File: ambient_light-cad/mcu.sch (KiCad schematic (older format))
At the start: 22 parts

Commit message: [Modified] +5V to VCC /interface
전에 USBVCC와 레귤레이터 5V 분리를 위해서 섞인 VCC와 +5V를 단일화 시킴
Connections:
- net labels removed: +5V
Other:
- moved on the sheet: C?, D?, SW?, U?, Y?

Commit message: [Modified] Register symbol
R_Small to R_Small_US (구불구불하게 생긴 기호)
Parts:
- added U?: NE555D, Package_SO:SOIC-8_3.9x4.9mm_P1.27mm, symbol Timer:NE555D
- R? (x6): symbol Device:R_Small -> Device:R_Small_US
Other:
- moved on the sheet: C?, Y?
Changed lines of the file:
@@
 L power:GND #PWR?
 U 1 1 5FD4BFB2
-P 7700 4250
+P 1950 7150
 AR Path="/5FD4BFB2" Ref="#PWR?"  Part="1"
 AR Path="/5FD145BE/5FD4BFB2" Ref="#PWR?"  Part="1"
-F 0 "#PWR?" H 7700 4000 50  0001 C CNN
-F 1 "GND" H 7705 4077 50  0000 C CNN
-F 2 "" H 7700 4250 50  0001 C CNN
-F 3 "" H 7700 4250 50  0001 C CNN
-	1    7700 4250
-	1    0    0    -1
-$EndComp
-Text Label 6700 3300 0    50   ~ 0
+F 0 "#PWR?" H 1950 6900 50  0001 C CNN
+F 1 "GND" H 1955 6977 50  0000 C CNN
+F 2 "" H 1950 7150 50  0001 C CNN
+F 3 "" H 1950 7150 50  0001 C CNN
+	1    1950 7150
+	1    0    0    -1
+$EndComp
+Text Label 950  6200 0    50   ~ 0
 XTAL1
-Text Label 6700 3400 0    50   ~ 0
+Text Label 950  6300 0    50   ~ 0
 XTAL2
 Wire Wire Line
-	7300 2900 7700 2900
-Wire Wire Line
-	7300 3300 6700 3300
-Wire Wire Line
-	7700 2900 7700 3400
-Wire Wire Line
-	7700 3400 6700 3400
-Connection ~ 7300 3300
-Connection ~ 7700 3400
-Wire Wire Line
-	7100 3100 7100 4050
-Wire Wire Line
-	7100 4050 7300 4050
-Connection ~ 7300 4050
-Wire Wire Line
-	7300 4050 7500 4050
-Wire Wire Line
-	7500 3100 7500 4050
-Connection ~ 7500 4050
-Wire Wire Line
-	7500 4050 7700 4050
-Wire Wire Line
-	7700 4050 7700 4250
-Connection ~ 7700 4050
+	1550 5800 1950 5800
+Wire Wire Line
+	1550 6200 950  6200
+Wire Wire Line
+	1950 5800 1950 6300
+Wire Wire Line
+	1950 6300 950  6300
+Connection ~ 1550 6200
+Connection ~ 1950 6300
+Wire Wire Line
+	1350 6000 1350 6950
+Wire Wire Line
+	1350 6950 1550 6950
+Connection ~ 1550 6950
+Wire Wire Line
+	1550 6950 1750 6950
+Wire Wire Line
+	1750 6000 1750 6950
+Connection ~ 1750 6950
+Wire Wire Line
+	1750 6950 1950 6950
+Wire Wire Line
+	1950 6950 1950 7150
+Connection ~ 1950 6950
 $Comp
 L Interface_USB:CH340G U?
@@
 $EndComp
 $Comp
-L Device:R_Small R?
+L Device:R_Small_US R?
 U 1 1 5FD4C06D
 P 3900 2000
@@
 L Device:Crystal_GND24_Small Y?
 U 1 1 5FD4C073
-P 7300 3100
+P 1550 6000
 AR Path="/5FD4C073" Ref="Y?"  Part="1"
 AR Path="/5FD145BE/5FD4C073" Ref="Y?"  Part="1"
-F 0 "Y?" V 7100 2600 50  0000 L CNN
-F 1 "14.4756MHz" V 7200 2600 50  0000 L CNN
-F 2 "" H 7300 3100 50  0001 C CNN
-F 3 "~" H 7300 3100 50  0001 C CNN
-	1    7300 3100
+F 0 "Y?" V 1350 5500 50  0000 L CNN
+F 1 "14.4756MHz" V 1450 5500 50  0000 L CNN
+F 2 "" H 1550 6000 50  0001 C CNN
+F 3 "~" H 1550 6000 50  0001 C CNN
+	1    1550 6000
 	0    1    1    0
 $EndComp
@@
 	0    -1   -1   0
 $EndComp
-$Comp
-L Device:R_Small R?
-U 1 1 5FD4C07F
-P 3900 2100
-AR Path="/5FD4C07F" Ref="R?"  Part="1"
-AR Path="/5FD145BE/5FD4C07F" Ref="R?"  Part="1"
-F 0 "R?" V 4000 2050 50  0000 C CNN
-F 1 "1k" V 4000 2150 50  0000 C CNN
-F 2 "" H 3900 2100 50  0001 C CNN
-F 3 "~" H 3900 2100 50  0001 C CNN
-	1    3900 2100
-	0    1    1    0
-$EndComp
 Wire Wire Line
 	3500 2000 3800 2000
@@
 	4000 2000 4150 2000
 $Comp
-L Device:R_Small R?
+L Device:R_Small_US R?
 U 1 1 5FD4C089
 P 4300 1300
@@
 $EndComp
 $Comp
-L Device:R_Small R?
+L Device:R_Small_US R?
 U 1 1 5FD4C08F
 P 4150 1300
@@
 	4150 1150 4150 1200
 $Comp
-L Device:R_Small R?
+L Device:R_Small_US R?
 U 1 1 5FD4C097
 P 5900 5250
@@
 Wire Wire Line
 	3500 2700 3700 2700
-Wire Wire Line
-	3900 2700 4100 2700
 $Comp
 L Device:C_Small C?
 U 1 1 5FD4C0D2
-P 7300 3700
+P 1550 6600
 AR Path="/5FD4C0D2" Ref="C?"  Part="1"
 AR Path="/5FD145BE/5FD4C0D2" Ref="C?"  Part="1"
-F 0 "C?" H 7400 3700 50  0000 L CNN
-F 1 "18pF" H 7300 3600 50  0000 L CNN
-F 2 "" H 7300 3700 50  0001 C CNN
-F 3 "~" H 7300 3700 50  0001 C CNN
-	1    7300 3700
+F 0 "C?" H 1650 6600 50  0000 L CNN
+F 1 "18pF" H 1550 6500 50  0000 L CNN
+F 2 "" H 1550 6600 50  0001 C CNN
+F 3 "~" H 1550 6600 50  0001 C CNN
+	1    1550 6600
 	1    0    0    -1
 $EndComp
@@
 L Device:C_Small C?
 U 1 1 5FD4C0D8
-P 7700 3700
+P 1950 6600
 AR Path="/5FD4C0D8" Ref="C?"  Part="1"
 AR Path="/5FD145BE/5FD4C0D8" Ref="C?"  Part="1"
-F 0 "C?" H 7800 3700 50  0000 L CNN
-F 1 "18pF" H 7700 3600 50  0000 L CNN
-F 2 "" H 7700 3700 50  0001 C CNN
-F 3 "~" H 7700 3700 50  0001 C CNN
-	1    7700 3700
-	1    0    0    -1
-$EndComp
-Wire Wire Line
-	7300 3300 7300 3600
-Wire Wire Line
-	7300 3800 7300 4050
-Wire Wire Line
-	7700 3400 7700 3600
-Wire Wire Line
-	7700 3800 7700 4050
-Wire Wire Line
-	7300 3200 7300 3300
-Wire Wire Line
-	7100 3100 7200 3100
-Wire Wire Line
-	7400 3100 7500 3100
-Wire Wire Line
-	7300 2900 7300 3000
+F 0 "C?" H 2050 6600 50  0000 L CNN
+F 1 "18pF" H 1950 6500 50  0000 L CNN
+F 2 "" H 1950 6600 50  0001 C CNN
+F 3 "~" H 1950 6600 50  0001 C CNN
+	1    1950 6600
+	1    0    0    -1
+$EndComp
+Wire Wire Line
+	1550 6200 1550 6500
+Wire Wire Line
+	1550 6700 1550 6950
+Wire Wire Line
+	1950 6300 1950 6500
+Wire Wire Line
+	1950 6700 1950 6950
+Wire Wire Line
+	1550 6100 1550 6200
+Wire Wire Line
+	1350 6000 1450 6000
+Wire Wire Line
+	1650 6000 1750 6000
+Wire Wire Line
+	1550 5800 1550 5900
 $Comp
 L Device:Crystal_GND24_Small Y?
@@
 	1650 1900 1750 1900
 $Comp
-L Device:R_Small R?
+L Device:R_Small_US R?
 U 1 1 5FD4C0F0
 P 1350 4100
@@
 	1    0    0    -1
 $EndComp
+$Comp
+L Timer:NE555D U?
+U 1 1 5FE4F839
+P 8100 2550
+F 0 "U?" H 7850 2150 50  0000 C CNN
+F 1 "NE555D" H 7850 2050 50  0000 C CNN
+F 2 "Package_SO:SOIC-8_3.9x4.9mm_P1.27mm" H 8950 2150 50  0001 C CNN
+F 3 "http://www.ti.com/lit/ds/symlink/ne555.pdf" H 8950 2150 50  0001 C CNN
+	1    8100 2550
+	1    0    0    -1
+$EndComp
+$Comp
+L power:VCC #PWR?
+U 1 1 5FE4FEF0
+P 8100 1750
+F 0 "#PWR?" H 8100 1600 50  0001 C CNN
+F 1 "VCC" H 8115 1923 50  0000 C CNN
+F 2 "" H 8100 1750 50  0001 C CNN
+F 3 "" H 8100 1750 50  0001 C CNN
+	1    8100 1750
+	1    0    0    -1
+$EndComp
+$Comp
+L power:GND #PWR?
+U 1 1 5FE50BA2
+P 8100 3150
+F 0 "#PWR?" H 8100 2900 50  0001 C CNN
+F 1 "GND" H 8105 2977 50  0000 C CNN
+F 2 "" H 8100 3150 50  0001 C CNN
+F 3 "" H 8100 3150 50  0001 C CNN
+	1    8100 3150
+	1    0    0    -1
+$EndComp
+Wire Wire Line
+	3900 2700 4100 2700
+$Comp
+L Device:R_Small_US R?
+U 1 1 5FD4C07F
+P 3900 2100
+AR Path="/5FD4C07F" Ref="R?"  Part="1"
+AR Path="/5FD145BE/5FD4C07F" Ref="R?"  Part="1"
+F 0 "R?" V 4000 2050 50  0000 C CNN
+F 1 "1k" V 4000 2150 50  0000 C CNN
+F 2 "" H 3900 2100 50  0001 C CNN
+F 3 "~" H 3900 2100 50  0001 C CNN
+	1    3900 2100
+	0    1    1    0
+$EndComp
 $EndSCHEMATC

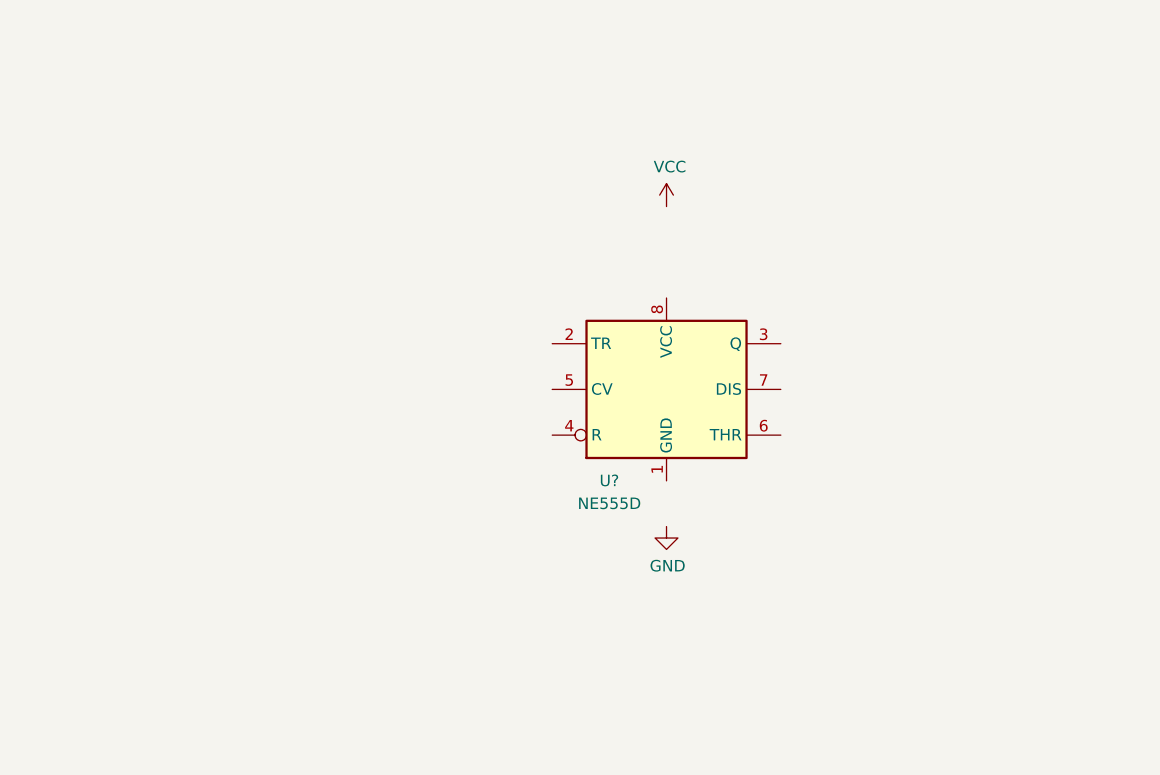
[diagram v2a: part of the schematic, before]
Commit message: [Added] NE555 Reset Setting button
CH340G DTR pin과 ATmega328P Rst pin 을 일시적으로 연결시키기 위한 10sec NE555 Monostable 로직 구현
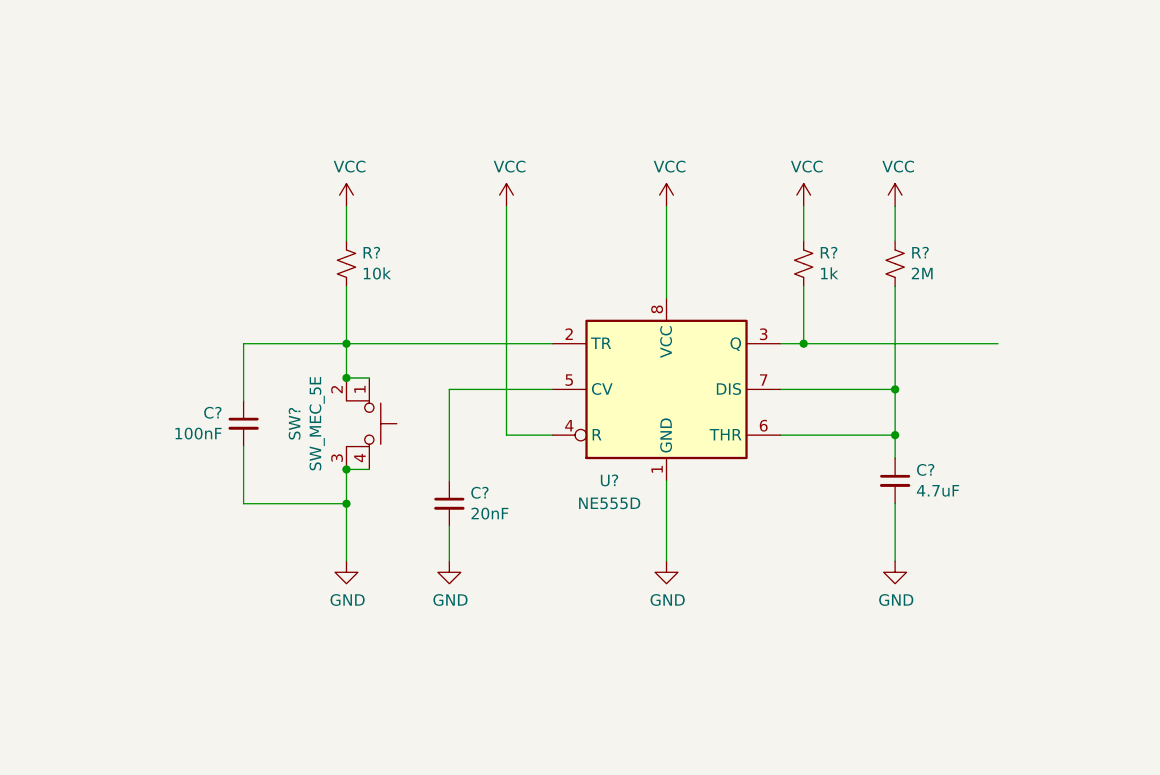
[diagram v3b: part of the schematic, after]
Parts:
- added C?: 20nF, symbol Device:C_Small
- added C?: 4.7uF, symbol Device:C_Small
- added C?: 100nF, symbol Device:C_Small
- added R?: 10k, symbol Device:R_Small_US
- added R?: 2M, symbol Device:R_Small_US
- added R?: 1k, symbol Device:R_Small_US
- added SW?: SW_MEC_5E, symbol Switch:SW_MEC_5E
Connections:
- net GND: now also U?.1 (GND), C?.2, C?.2, C?.2, SW?.3 (K), SW?.4 (A)
- net VCC: now also U?.4 (R), U?.8 (VCC), R?.1, R?.1, R?.1
- net at U?.2 (TR): now also C?.1, R?.2, SW?.1, SW?.2
- net at U?.3 (Q): now also R?.2
- net at U?.5 (CV): now also C?.1
- net at U?.6 (THR): now also U?.7 (DIS), C?.1, R?.2
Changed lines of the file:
@@
-$EndComp
-$Comp
-L Timer:NE555D U?
-U 1 1 5FE4F839
-P 8100 2550
-F 0 "U?" H 7850 2150 50  0000 C CNN
-F 1 "NE555D" H 7850 2050 50  0000 C CNN
-F 2 "Package_SO:SOIC-8_3.9x4.9mm_P1.27mm" H 8950 2150 50  0001 C CNN
-F 3 "http://www.ti.com/lit/ds/symlink/ne555.pdf" H 8950 2150 50  0001 C CNN
-	1    8100 2550
-	1    0    0    -1
 $EndComp
 $Comp
@@
 L power:GND #PWR?
 U 1 1 5FE50BA2
-P 8100 3150
-F 0 "#PWR?" H 8100 2900 50  0001 C CNN
-F 1 "GND" H 8105 2977 50  0000 C CNN
-F 2 "" H 8100 3150 50  0001 C CNN
-F 3 "" H 8100 3150 50  0001 C CNN
-	1    8100 3150
+P 8100 3300
+F 0 "#PWR?" H 8100 3050 50  0001 C CNN
+F 1 "GND" H 8105 3127 50  0000 C CNN
+F 2 "" H 8100 3300 50  0001 C CNN
+F 3 "" H 8100 3300 50  0001 C CNN
+	1    8100 3300
 	1    0    0    -1
 $EndComp
@@
 	0    1    1    0
 $EndComp
+$Comp
+L Device:R_Small_US R?
+U 1 1 5FE64F71
+P 6700 2000
+F 0 "R?" H 6768 2046 50  0000 L CNN
+F 1 "10k" H 6768 1955 50  0000 L CNN
+F 2 "" H 6700 2000 50  0001 C CNN
+F 3 "~" H 6700 2000 50  0001 C CNN
+	1    6700 2000
+	1    0    0    -1
+$EndComp
+$Comp
+L Device:C_Small C?
+U 1 1 5FE7649B
+P 7150 3050
+F 0 "C?" H 7242 3096 50  0000 L CNN
+F 1 "20nF" H 7242 3005 50  0000 L CNN
+F 2 "" H 7150 3050 50  0001 C CNN
+F 3 "~" H 7150 3050 50  0001 C CNN
+	1    7150 3050
+	1    0    0    -1
+$EndComp
+$Comp
+L Device:R_Small_US R?
+U 1 1 5FE80D08
+P 8700 2000
+F 0 "R?" H 8768 2046 50  0000 L CNN
+F 1 "1k" H 8768 1955 50  0000 L CNN
+F 2 "" H 8700 2000 50  0001 C CNN
+F 3 "~" H 8700 2000 50  0001 C CNN
+	1    8700 2000
+	1    0    0    -1
+$EndComp
+Wire Wire Line
+	8100 2950 8100 3300
+$Comp
+L power:GND #PWR?
+U 1 1 5FEB39CC
+P 7150 3300
+F 0 "#PWR?" H 7150 3050 50  0001 C CNN
+F 1 "GND" H 7155 3127 50  0000 C CNN
+F 2 "" H 7150 3300 50  0001 C CNN
+F 3 "" H 7150 3300 50  0001 C CNN
+	1    7150 3300
+	1    0    0    -1
+$EndComp
+Wire Wire Line
+	7150 3300 7150 3150
+Wire Wire Line
+	7150 2950 7150 2550
+$Comp
+L Switch:SW_MEC_5E SW?
+U 1 1 5FE63505
+P 6700 2700
+F 0 "SW?" H 6700 2475 50  0000 C CNN
+F 1 "SW_MEC_5E" H 6700 2566 50  0000 C CNN
+F 2 "" H 6700 3000 50  0001 C CNN
+F 3 "http://www.apem.com/int/index.php?controller=attachment&id_attachment=1371" H 6700 3000 50  0001 C CNN
+	1    6700 2700
+	0    1    1    0
+$EndComp
+$Comp
+L Timer:NE555D U?
+U 1 1 5FE4F839
+P 8100 2550
+F 0 "U?" H 7850 2150 50  0000 C CNN
+F 1 "NE555D" H 7850 2050 50  0000 C CNN
+F 2 "Package_SO:SOIC-8_3.9x4.9mm_P1.27mm" H 8950 2150 50  0001 C CNN
+F 3 "http://www.ti.com/lit/ds/symlink/ne555.pdf" H 8950 2150 50  0001 C CNN
+	1    8100 2550
+	1    0    0    -1
+$EndComp
+Wire Wire Line
+	8100 1750 8100 2150
+Wire Wire Line
+	6700 2100 6700 2350
+Wire Wire Line
+	7600 2350 6700 2350
+Connection ~ 6700 2350
+Wire Wire Line
+	6700 2350 6700 2500
+$Comp
+L power:GND #PWR?
+U 1 1 5FF1BCD1
+P 6700 3300
+F 0 "#PWR?" H 6700 3050 50  0001 C CNN
+F 1 "GND" H 6705 3127 50  0000 C CNN
+F 2 "" H 6700 3300 50  0001 C CNN
+F 3 "" H 6700 3300 50  0001 C CNN
+	1    6700 3300
+	1    0    0    -1
+$EndComp
+Wire Wire Line
+	6700 2900 6700 3050
+$Comp
+L power:VCC #PWR?
+U 1 1 5FF26EBE
+P 6700 1750
+F 0 "#PWR?" H 6700 1600 50  0001 C CNN
+F 1 "VCC" H 6715 1923 50  0000 C CNN
+F 2 "" H 6700 1750 50  0001 C CNN
+F 3 "" H 6700 1750 50  0001 C CNN
+	1    6700 1750
+	1    0    0    -1
+$EndComp
+Wire Wire Line
+	6700 1750 6700 1900
+Wire Wire Line
+	6700 2500 6800 2500
+Connection ~ 6700 2500
+Wire Wire Line
+	6700 2900 6800 2900
+Connection ~ 6700 2900
+$Comp
+L Device:C_Small C?
+U 1 1 5FF36A63
+P 6250 2700
+F 0 "C?" H 6342 2746 50  0000 L CNN
+F 1 "100nF" H 6342 2655 50  0000 L CNN
+F 2 "" H 6250 2700 50  0001 C CNN
+F 3 "~" H 6250 2700 50  0001 C CNN
+	1    6250 2700
+	-1   0    0    -1
+$EndComp
+Wire Wire Line
+	6250 2800 6250 3050
+Wire Wire Line
+	6250 3050 6700 3050
+Connection ~ 6700 3050
+Wire Wire Line
+	6700 3050 6700 3300
+Wire Wire Line
+	6250 2600 6250 2350
+Wire Wire Line
+	6250 2350 6700 2350
+$Comp
+L power:VCC #PWR?
+U 1 1 5FF5892D
+P 7400 1750
+F 0 "#PWR?" H 7400 1600 50  0001 C CNN
+F 1 "VCC" H 7415 1923 50  0000 C CNN
+F 2 "" H 7400 1750 50  0001 C CNN
+F 3 "" H 7400 1750 50  0001 C CNN
+	1    7400 1750
+	1    0    0    -1
+$EndComp
+Wire Wire Line
+	7150 2550 7600 2550
+Wire Wire Line
+	7400 2750 7600 2750
+Wire Wire Line
+	7400 1750 7400 2750
+$Comp
+L power:VCC #PWR?
+U 1 1 5FF698E0
+P 8700 1750
+F 0 "#PWR?" H 8700 1600 50  0001 C CNN
+F 1 "VCC" H 8715 1923 50  0000 C CNN
+F 2 "" H 8700 1750 50  0001 C CNN
+F 3 "" H 8700 1750 50  0001 C CNN
+	1    8700 1750
+	1    0    0    -1
+$EndComp
+Wire Wire Line
+	8700 1900 8700 1750
+Wire Wire Line
+	8700 2100 8700 2350
+Connection ~ 8700 2350
+Wire Wire Line
+	8700 2350 8600 2350
+Wire Wire Line
+	8700 2350 9550 2350
+Wire Wire Line
+	9100 3050 9100 3300
+Wire Wire Line
+	9100 2750 9100 2850
+Connection ~ 9100 2750
+Wire Wire Line
+	9100 2550 9100 2750
+Wire Wire Line
+	8600 2750 9100 2750
+Wire Wire Line
+	8600 2550 9100 2550
+$Comp
+L power:GND #PWR?
+U 1 1 5FE84EAC
+P 9100 3300
+F 0 "#PWR?" H 9100 3050 50  0001 C CNN
+F 1 "GND" H 9105 3127 50  0000 C CNN
+F 2 "" H 9100 3300 50  0001 C CNN
+F 3 "" H 9100 3300 50  0001 C CNN
+	1    9100 3300
+	1    0    0    -1
+$EndComp
+$Comp
+L Device:C_Small C?
+U 1 1 5FE7A68B
+P 9100 2950
+F 0 "C?" H 9192 2996 50  0000 L CNN
+F 1 "4.7uF" H 9192 2905 50  0000 L CNN
+F 2 "" H 9100 2950 50  0001 C CNN
+F 3 "~" H 9100 2950 50  0001 C CNN
+	1    9100 2950
+	1    0    0    -1
+$EndComp
+Connection ~ 9100 2550
+Wire Wire Line
+	9100 2100 9100 2550
+Wire Wire Line
+	9100 1900 9100 1750
+$Comp
+L power:VCC #PWR?
+U 1 1 5FF426CD
+P 9100 1750
+F 0 "#PWR?" H 9100 1600 50  0001 C CNN
+F 1 "VCC" H 9115 1923 50  0000 C CNN
+F 2 "" H 9100 1750 50  0001 C CNN
+F 3 "" H 9100 1750 50  0001 C CNN
+	1    9100 1750
+	1    0    0    -1
+$EndComp
+$Comp
+L Device:R_Small_US R?
+U 1 1 5FE7DB2C
+P 9100 2000
+F 0 "R?" H 9168 2046 50  0000 L CNN
+F 1 "2M" H 9168 1955 50  0000 L CNN
+F 2 "" H 9100 2000 50  0001 C CNN
+F 3 "~" H 9100 2000 50  0001 C CNN
+	1    9100 2000
+	1    0    0    -1
+$EndComp
 $EndSCHEMATC
